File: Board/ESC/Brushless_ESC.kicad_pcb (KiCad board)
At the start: 2 copper layers, 63 x 36 mm, 77 parts, among them IC1 ATMEGA88PA-A, P1 Battery+, P10 MISO, P11 Reset, P12 SCK, P13 Gnd, P2 Battery-, P3 Coil_A, P4 Sup, P5 Coil_B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

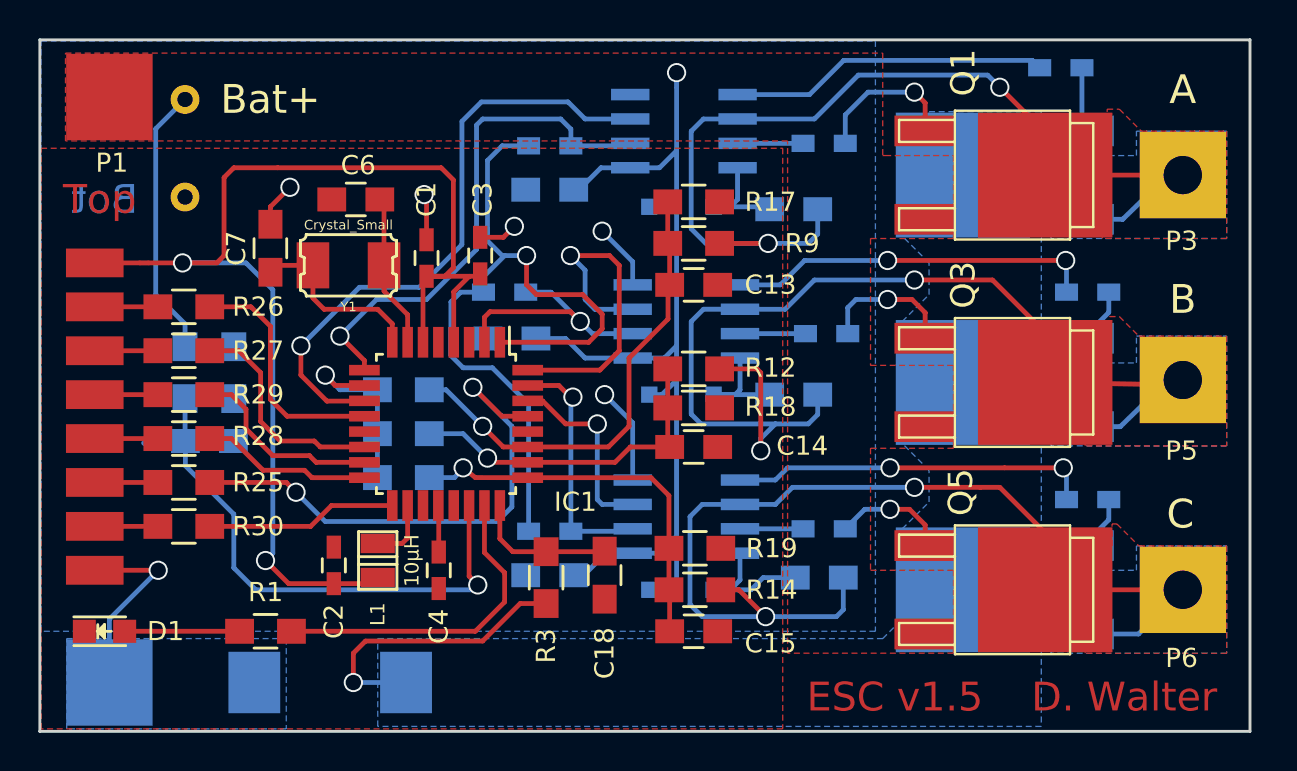
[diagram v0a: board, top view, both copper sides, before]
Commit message: Repaired Repository, Fixed wrong footprint of FETs
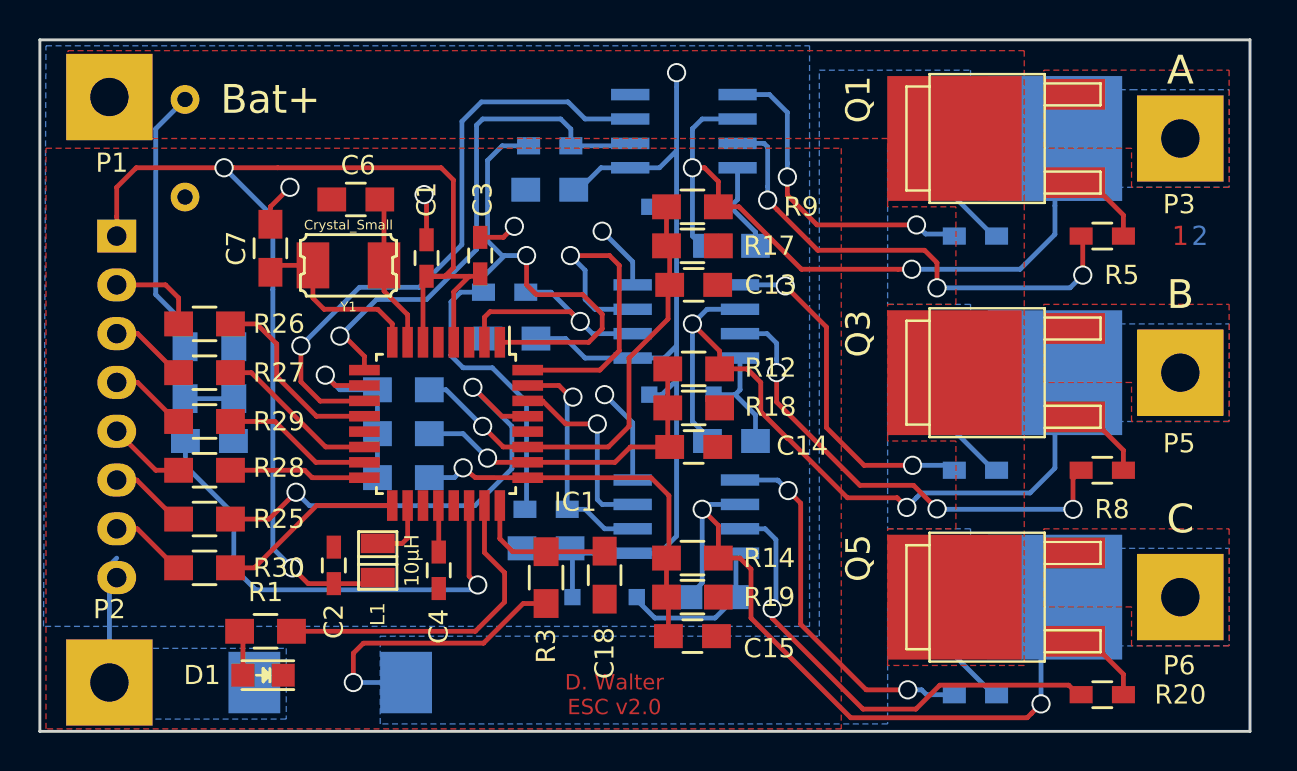
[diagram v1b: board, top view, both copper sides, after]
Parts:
- removed P10: MISO, Wire_Pads:SolderWirePad_single_0-8mmDrill
- removed P11: Reset, Wire_Pads:SolderWirePad_single_0-8mmDrill
- removed P12: SCK, Wire_Pads:SolderWirePad_single_0-8mmDrill
- removed P13: Gnd, Wire_Pads:SolderWirePad_single_0-8mmDrill
- removed P7: PPM, Wire_Pads:SolderWirePad_single_0-8mmDrill
- removed P8: SS, Wire_Pads:SolderWirePad_single_0-8mmDrill
- removed P9: MOSI, Wire_Pads:SolderWirePad_single_0-8mmDrill
- P4: value Sup -> CONN_01X08; footprint Wire_Pads:SolderWirePad_single_0-8mmDrill -> Pin_Headers:Pin_Header_Angled_1x08; moved to B.Cu
- R20, R5, R8: moved to F.Cu
- moved R20 16.9 mm to (171.6, 93.1)
- moved R8 16.0 mm to (171.6, 81.4)
- moved R5 15.3 mm to (171.6, 69.2)
- moved R24 11.7 mm to (165.0, 93.1)
- moved R16 11.0 mm to (165.0, 81.4)
- moved R7 9.83 mm to (165.0, 69.2)
- moved D1 8.57 mm to (128.0, 92.1), turned to 180 degrees
- moved C16 5.68 mm to (151.3, 88.0), turned to 180 degrees
- moved C12 4.04 mm to (152.3, 79.9), turned to 180 degrees
- moved D6 4.02 mm to (145.7, 88.0)
- moved C11 3.76 mm to (152.3, 69.7), turned to 180 degrees
- moved R19 2.54 mm to (150.3, 88.0)
- moved Q1 2.44 mm to (167.1, 64.1), turned to 90 degrees
- moved R30 2.41 mm to (124.9, 86.5)
- moved Q2 2.40 mm to (166.1, 64.1), turned to 90 degrees
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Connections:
- C11 pad 2: COIL_A -> /Power/Coil_A
- C12 pad 2: COIL_B -> /Power/Coil_B
- C16 pad 2: COIL_C -> /Power/Coil_C
- P3 pad 1: COIL_A -> /Power/Coil_A
- P5 pad 1: COIL_B -> /Power/Coil_B
- P6 pad 1: COIL_C -> /Power/Coil_C
- Q1 pad 2: COIL_A -> +BATT
- Q1 pad 3: +BATT -> /Power/Coil_A
- Q2 pad 2: FET_Drain -> /Power/Coil_A
- Q2 pad 3: COIL_A -> Net-(Q2-Pad3)
- Q3 pad 2: COIL_B -> +BATT
- Q3 pad 3: +BATT -> /Power/Coil_B
- Q4 pad 2: FET_Drain -> /Power/Coil_B
- Q4 pad 3: COIL_B -> Net-(Q2-Pad3)
- Q5 pad 2: COIL_C -> +BATT
- Q5 pad 3: +BATT -> /Power/Coil_C
- Q6 pad 2: FET_Drain -> /Power/Coil_C
- Q6 pad 3: COIL_C -> Net-(Q2-Pad3)
- R12 pad 2: COIL_B -> /Power/Coil_B
- R14 pad 2: COIL_C -> /Power/Coil_C
- R3 pad 1: FET_Drain -> Net-(Q2-Pad3)
- R4 pad 2: FET_Drain -> Net-(Q2-Pad3)
- R9 pad 2: COIL_A -> /Power/Coil_A
- U2 pad 6: COIL_A -> /Power/Coil_A
- U3 pad 6: COIL_B -> /Power/Coil_B
- U4 pad 6: COIL_C -> /Power/Coil_C
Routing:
- net COIL_B: track 61.9 -> 0.00 mm, vias 2 -> 0
- net COIL_C: track 56.9 -> 0.00 mm, vias 2 -> 0
- net COIL_A: track 54.6 -> 0.00 mm, vias 2 -> 0
- net /Power/Coil_B: track 0.00 -> 40.4 mm, vias 0 -> 2
- net /Power/Coil_C: track 0.00 -> 37.7 mm, vias 0 -> 2
- net /Power/Coil_A: track 0.00 -> 37.0 mm, vias 0 -> 2
- net Net-(R5-Pad2): track 3.41 -> 25.8 mm, vias 0 -> 3
- net Net-(R8-Pad2): track 3.41 -> 25.1 mm, vias 0 -> 3
- net Net-(R20-Pad2): track 3.46 -> 25.0 mm, vias 0 -> 1
- net FET_Drain: track 15.4 -> 0.00 mm, vias 1 -> 0
- net Net-(Q2-Pad3): track 0.00 -> 15.4 mm, vias 0 -> 1
- net Net-(IC1-Pad12): track 13.9 -> 9.96 mm
- net GND: track 25.8 -> 22.0 mm, vias 6 -> 5
- net Net-(D1-Pad2): track 5.98 -> 2.36 mm
- net Net-(Q1-Pad1): track 8.16 -> 4.56 mm, vias 1 -> 0
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- added copper zone on B.Cu, net /Power/Coil_A
- added copper zone on F.Cu, net /Power/Coil_A
- added copper zone on B.Cu, net /Power/Coil_B
- added copper zone on F.Cu, net /Power/Coil_B
- added copper zone on B.Cu, net /Power/Coil_C
- added copper zone on F.Cu, net /Power/Coil_C
- added copper zone on B.Cu, net Net-(Q2-Pad3)
- removed copper zone on B.Cu, net COIL_A
- removed copper zone on F.Cu, net COIL_A
- removed copper zone on B.Cu, net COIL_B
- removed copper zone on F.Cu, net COIL_B
- removed copper zone on B.Cu, net COIL_C
- removed copper zone on F.Cu, net COIL_C
- removed copper zone on B.Cu, net FET_Drain
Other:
- board text added: "1"
- board text added: "2"
- board text added: "D. Walter ESC v2.0"
- board text removed: "Bot"
- board text removed: "D. Walter"
- board text removed: "ESC v1.5"
- board text removed: "Top"

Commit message: Temperaturmessung hinzugefügt
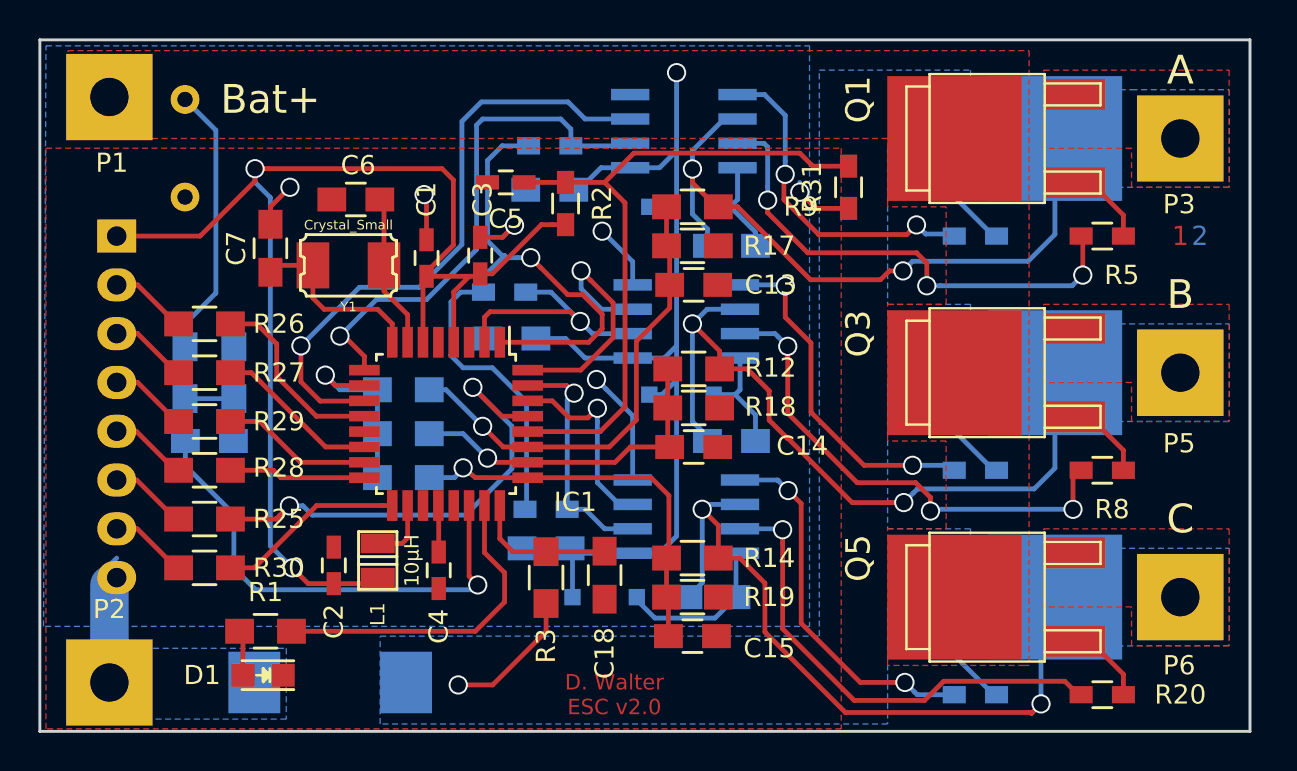
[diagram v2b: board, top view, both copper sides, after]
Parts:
- added C5: 100nF, Capacitors_SMD:C_0603_HandSoldering, F.Cu at (140.6, 66.4)
- added R2: 1k5, Resistors_SMD:R_0603_HandSoldering, F.Cu at (143.7, 67.5)
- added R31: 470R, Resistors_SMD:R_0603_HandSoldering, F.Cu at (158.4, 66.7)
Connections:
- IC1 pad 28: (no net) -> /Controller/T_Sense
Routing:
- net /Controller/T_Sense: track 0.00 -> 35.5 mm
- net Net-(Q2-Pad3): track 15.4 -> 7.18 mm
- net /Controller//SD_B: track 17.7 -> 13.4 mm
- net GND: track 22.0 -> 25.9 mm, vias 5 -> 6
- net +5V: track 63.8 -> 66.9 mm
- net /Controller/PWM: track 39.3 -> 38.4 mm
- net /Controller/PPM: track 4.85 -> 4.06 mm
- net /Power/Coil_A: track 37.0 -> 36.2 mm
- net Net-(R8-Pad2): track 25.1 -> 25.9 mm
- net Net-(R7-Pad2): track 16.9 -> 17.4 mm

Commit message: Layoutänderung
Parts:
- added G***: LOGO, Loewe:Loewe_Klein, B.Cu at (133.5, 63.9)
- moved R31 9.15 mm to (158.7, 75.8)
- moved C5 3.84 mm to (144.2, 67.7), turned to 270 degrees
- moved R2 3.00 mm to (140.9, 66.4), turned to 180 degrees
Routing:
- net /Controller/T_Sense: track 35.5 -> 49.8 mm
- net GND: track 25.9 -> 35.4 mm
- net /Controller/IN_A: track 27.7 -> 24.6 mm
- net /Controller//SD_A: track 32.9 -> 30.1 mm
- net Net-(R7-Pad2): track 17.4 -> 15.6 mm
- net +5V: track 66.9 -> 65.5 mm
- net Net-(IC1-Pad29): track 24.7 -> 24.0 mm
- net /Controller/PWM: track 38.4 -> 37.8 mm
- net /Controller//SD_B: track 13.4 -> 12.7 mm
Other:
- net class Default: via_dia 1 -> 0.6; via_drill 0.8 -> 0.4

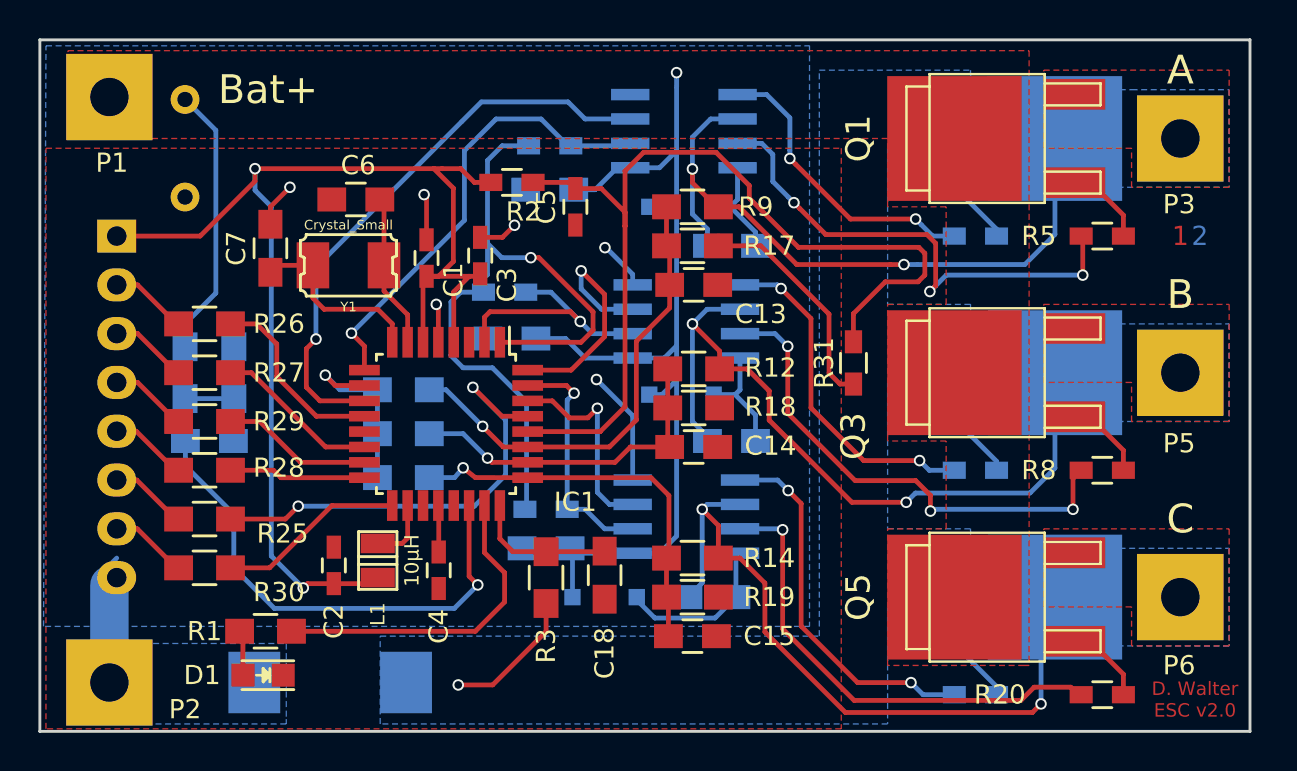
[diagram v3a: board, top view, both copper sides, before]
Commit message: BEC eingebaut, Interface auf I2C umgestellt, Zenderdioden
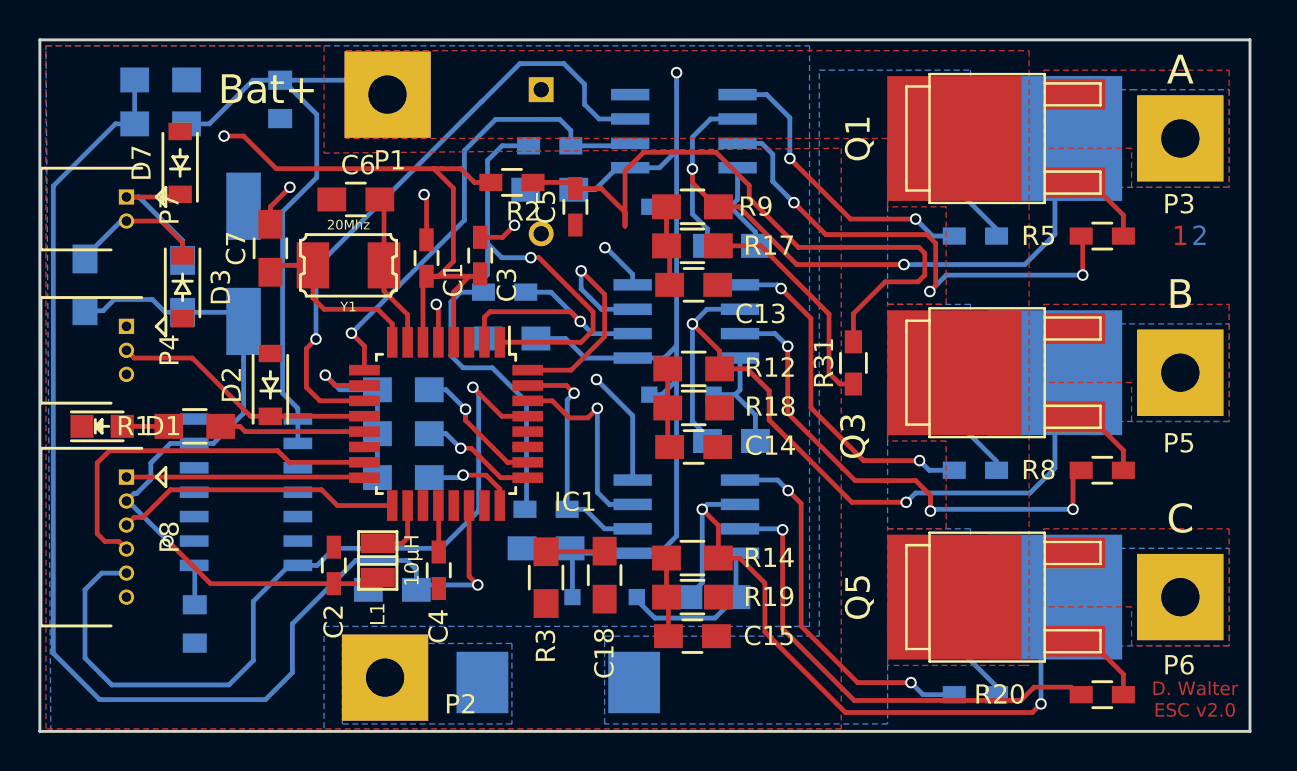
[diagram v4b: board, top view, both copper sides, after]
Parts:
- removed G***: LOGO, Loewe:Loewe_Klein
- removed R27, R28, R29, R30: 1k, Resistors_SMD:R_0805_HandSoldering
- added C20: 470nF, Capacitors_SMD:C_0805, B.Cu at (128.8, 62.1)
- added C21: 22µF, Capacitors_Tantalum_SMD:TantalC_SizeC_EIA-6032_HandSoldering, B.Cu at (126.9, 70.7)
- added C22: 100nF, Capacitors_SMD:C_0805, B.Cu at (124.4, 89.4)
- added D2: ZENER, Diodes_SMD:SOD-123, F.Cu at (128.3, 77.0)
- added D3: ZENER, Diodes_SMD:SOD-123, F.Cu at (123.8, 71.9)
- added D7: ZENER, Diodes_SMD:SOD-123, F.Cu at (123.6, 65.4)
- added P7: I2C, Connectors_Molex:Molex_PicoBlade_53048-0210, F.Cu at (120.8, 67.2)
- added P8: ISP, Connectors_Molex:Molex_PicoBlade_53048-0610, F.Cu at (120.8, 81.8)
- added U1: TLE4267, Housings_SOIC:SOIC-14_3.9x8.7mm_Pitch1.27mm, B.Cu at (127.1, 82.5)
- C19: footprint Capacitors_Elko_ThroughHole:Elko_vert_20x10mm_RM5 -> Capacitors_ThroughHole:C_Radial_D10_L20_P7.5
- P4: value CONN_01X08 -> PPM; footprint Pin_Headers:Pin_Header_Angled_1x08 -> Connectors_Molex:Molex_PicoBlade_53048-0310; moved to F.Cu
- R25, R26: value 1k -> 220R; moved to B.Cu
- Y1: value Crystal_Small -> 20Mhz
- moved C19 18.5 mm to (142.4, 61.6)
- moved R23 15.7 mm to (122.6, 61.1), turned to 180 degrees
- moved D1 15.4 mm to (119.6, 79.1), turned to 0 degrees
- moved P1 14.5 mm to (134.4, 61.8)
- moved P2 14.4 mm to (134.3, 92.2)
- moved R25 13.7 mm to (118.7, 71.8), turned to 270 degrees
- moved R22 13.0 mm to (122.6, 63.4), turned to 0 degrees
- moved C17 12.3 mm to (134.7, 87.6), turned to 180 degrees
- moved R4 11.9 mm to (143.3, 92.5)
- moved R1 11.3 mm to (124.4, 79.1)
- moved P4 4.73 mm to (120.8, 73.9), turned to 270 degrees
- moved R26 2.26 mm to (123.8, 71.8), turned to 270 degrees
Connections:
- IC1 pad 12: Net-(IC1-Pad12) -> /Controller/PPM
- IC1 pad 13: (no net) -> Net-(IC1-Pad13)
- IC1 pad 14: Net-(IC1-Pad14) -> (no net)
- IC1 pad 19: (no net) -> /Controller/T_Sense
- IC1 pad 23: Net-(IC1-Pad23) -> /Controller/BatCurrent+
- IC1 pad 24: /Controller/BatCurrent+ -> /Controller/BEMF_C
- IC1 pad 25: /Controller/BEMF_C -> /Controller/BEMF_B
- IC1 pad 26: /Controller/BEMF_B -> /Controller/BEMF_A
- IC1 pad 27: /Controller/BEMF_A -> /Controller/SDA
- IC1 pad 28: /Controller/T_Sense -> /Controller/SCL
- IC1 pad 29: Net-(IC1-Pad29) -> /Controller/Reset
- P4 pad 1: +5V -> GND
- P4 pad 3: /Controller/SS -> +5V
- R1 pad 2: Net-(IC1-Pad23) -> Net-(IC1-Pad13)
- R25 pad 1: Net-(IC1-Pad29) -> /Controller/SDA
- R25 pad 2: /Controller/Reset -> +5V
- R26 pad 1: /Controller/PPM -> /Controller/SCL
- R26 pad 2: Net-(IC1-Pad12) -> +5V
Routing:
- net /Controller/Reset: track 4.06 -> 42.7 mm, vias 0 -> 1
- net /Controller/V_Bat: track 30.8 -> 65.4 mm
- net Net-(IC1-Pad29): track 24.0 -> 0.00 mm, vias 2 -> 0
- net +BATT: track 65.6 -> 84.0 mm
- net Net-(IC1-Pad23): track 17.2 -> 0.00 mm
- net /Controller/T_Sense: track 49.8 -> 34.8 mm
- net /Controller/BEMF_A: track 25.5 -> 11.9 mm
- net /Controller/BEMF_C: track 21.4 -> 9.17 mm
- net Net-(IC1-Pad15): track 7.85 -> 20.0 mm
- net Net-(IC1-Pad12): track 9.96 -> 0.00 mm
- net /Controller/PPM: track 4.06 -> 13.8 mm
- net Net-(IC1-Pad14): track 8.57 -> 0.00 mm
- net /Controller/SDA: track 0.00 -> 7.92 mm
- net /Controller/SCL: track 0.00 -> 7.75 mm
- net /Controller/BEMF_B: track 18.1 -> 10.5 mm
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
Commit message: Layoutänderungen
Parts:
- removed R25, R26: 220R, Resistors_SMD:R_0805_HandSoldering
- C19: moved to F.Cu
- D1, D3: moved to B.Cu
- moved C5 25.8 mm to (139.0, 93.0), turned to 180 degrees
- moved R2 24.8 mm to (139.0, 91.2)
- moved D1 13.2 mm to (119.7, 92.3)
- moved R6 11.7 mm to (134.0, 72.1), turned to 0 degrees
- moved D2 4.16 mm to (124.5, 75.3)
- moved D3 3.49 mm to (120.3, 71.2), turned to 180 degrees
- moved L1 2.93 mm to (131.0, 86.4)
- moved R21 2.92 mm to (142.7, 80.5), turned to 90 degrees
- moved C2 2.79 mm to (128.8, 86.4)
- moved R23 2.69 mm to (122.2, 63.8)
- moved R1 2.43 mm to (126.8, 79.4)
- moved R22 1.94 mm to (122.2, 61.5)
- moved C17 1.53 mm to (135.3, 86.2), turned to 0 degrees
- moved D7 1.45 mm to (124.8, 66.3), turned to 0 degrees
- moved P2 1.27 mm to (133.0, 92.2)
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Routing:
- net /Controller/SDA: track 7.92 -> 30.8 mm, vias 0 -> 2
- net /Controller/T_Sense: track 34.8 -> 57.3 mm, vias 0 -> 4
- net /Controller/SCL: track 7.75 -> 29.1 mm, vias 0 -> 2
- net Net-(D1-Pad2): track 2.43 -> 18.8 mm, vias 0 -> 1
- net +5V: track 69.1 -> 84.3 mm
- net /Controller/BEMF_A: track 11.9 -> 25.4 mm
- net /Controller/Reset: track 42.7 -> 31.6 mm, vias 1 -> 2
- net /Controller/BEMF_C: track 9.17 -> 20.2 mm
- net /Controller/PWM: track 37.8 -> 29.9 mm
- net /Controller/BEMF_B: track 10.5 -> 18.1 mm
- net Net-(Q2-Pad3): track 0.00 -> 7.51 mm, vias 0 -> 1
- net /Controller/V_Bat: track 65.4 -> 60.0 mm, vias 1 -> 5
- net /Controller/BatCurrent+: track 3.06 -> 7.88 mm
- net GND: track 29.3 -> 26.5 mm
- net Net-(IC1-Pad13): track 7.59 -> 5.08 mm
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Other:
- board text added: "D. Walter ESC v2.1"
- board text removed: "D. Walter ESC v2.0"

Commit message: Layoutoptimierung
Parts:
- moved C2 6.24 mm to (135.1, 86.9), turned to 270 degrees
- moved L1 4.24 mm to (126.8, 85.7), turned to 180 degrees
- moved D7 3.59 mm to (122.2, 63.8)
- moved D2 3.00 mm to (123.8, 72.4)
- moved C4 1.09 mm to (138.9, 87.0), turned to 0 degrees
- moved R10 0.85 mm to (134.7, 79.0)
- moved R13 0.85 mm to (134.7, 81.2)
- moved R15 0.85 mm to (134.7, 83.3)
- moved C17 0.81 mm to (134.7, 85.7), turned to 180 degrees
- moved P5 0.76 mm to (175.7, 75.6)
- moved Q3 0.76 mm to (167.1, 75.6)
- moved Q4 0.76 mm to (166.1, 75.6)
- moved P6 0.63 mm to (175.7, 87.4)
- moved Q5 0.63 mm to (167.1, 87.4)
- moved Q6 0.63 mm to (166.1, 87.4)
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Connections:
- C2 pad 1: +5V -> Net-(C2-Pad1)
- IC1 pad 18: Net-(IC1-Pad18) -> Net-(C2-Pad1)
- L1 pad 1: Net-(IC1-Pad18) -> Net-(C2-Pad1)
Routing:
- net +5V: track 84.3 -> 69.7 mm
- net Net-(C2-Pad1): track 0.00 -> 10.3 mm
- net /Controller/Reset: track 31.6 -> 37.8 mm
- net Net-(IC1-Pad18): track 5.67 -> 0.00 mm
- net /Controller/V_Bat: track 60.0 -> 55.4 mm
- net /Controller/SCL: track 29.1 -> 33.5 mm
- net /Controller/SDA: track 30.8 -> 33.7 mm
- net /Controller/PPM: track 13.9 -> 16.5 mm
- net /Controller/BEMF_B: track 18.1 -> 20.0 mm
- net /Controller/BEMF_C: track 20.2 -> 22.1 mm
- net /Controller/IN_A: track 24.5 -> 22.9 mm
- net Net-(C4-Pad1): track 5.35 -> 4.10 mm
- net Net-(Q6-Pad1): track 4.61 -> 5.74 mm
- net /Power/Coil_A: track 35.8 -> 36.9 mm
- net Net-(R7-Pad2): track 15.6 -> 16.7 mm
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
